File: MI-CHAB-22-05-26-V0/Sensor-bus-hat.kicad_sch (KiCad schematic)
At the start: 45 parts, among them J6 Coaxial_Small, Q2 IRLML6244, U1 MS860702BA01-50, U2 LMT84DCK, U3 BNO085, U4 AP2112K-1.8, U5 LMT84DCK, U6 TPS3850H50DRCR, U7 MAX-M10M-00B, Y1 9HT10-32.768KBZF-T

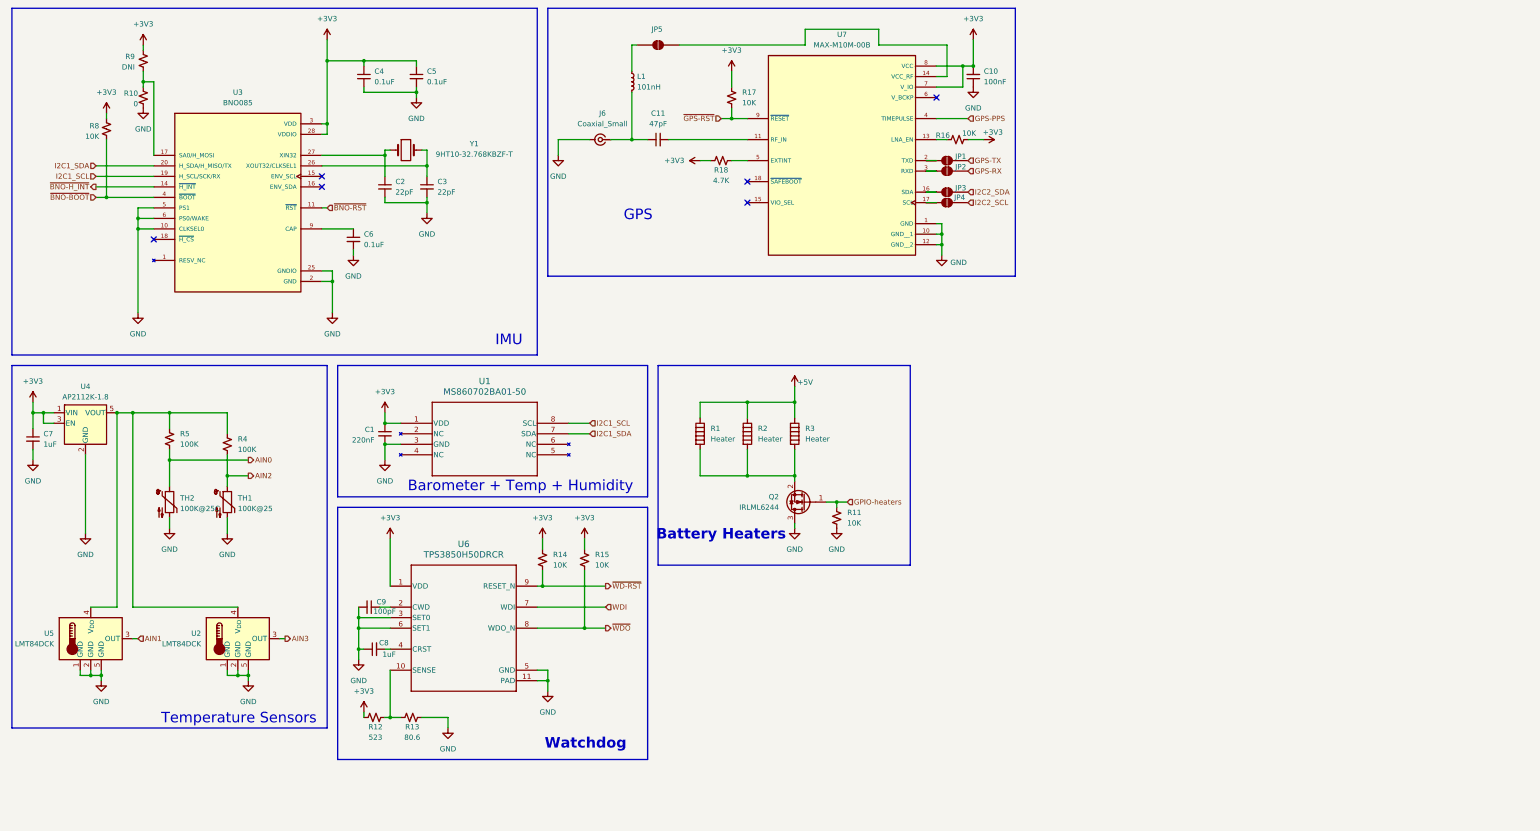
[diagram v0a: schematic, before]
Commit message: revision 0.1 - added debug stuff, CAN interface, I2C buffer
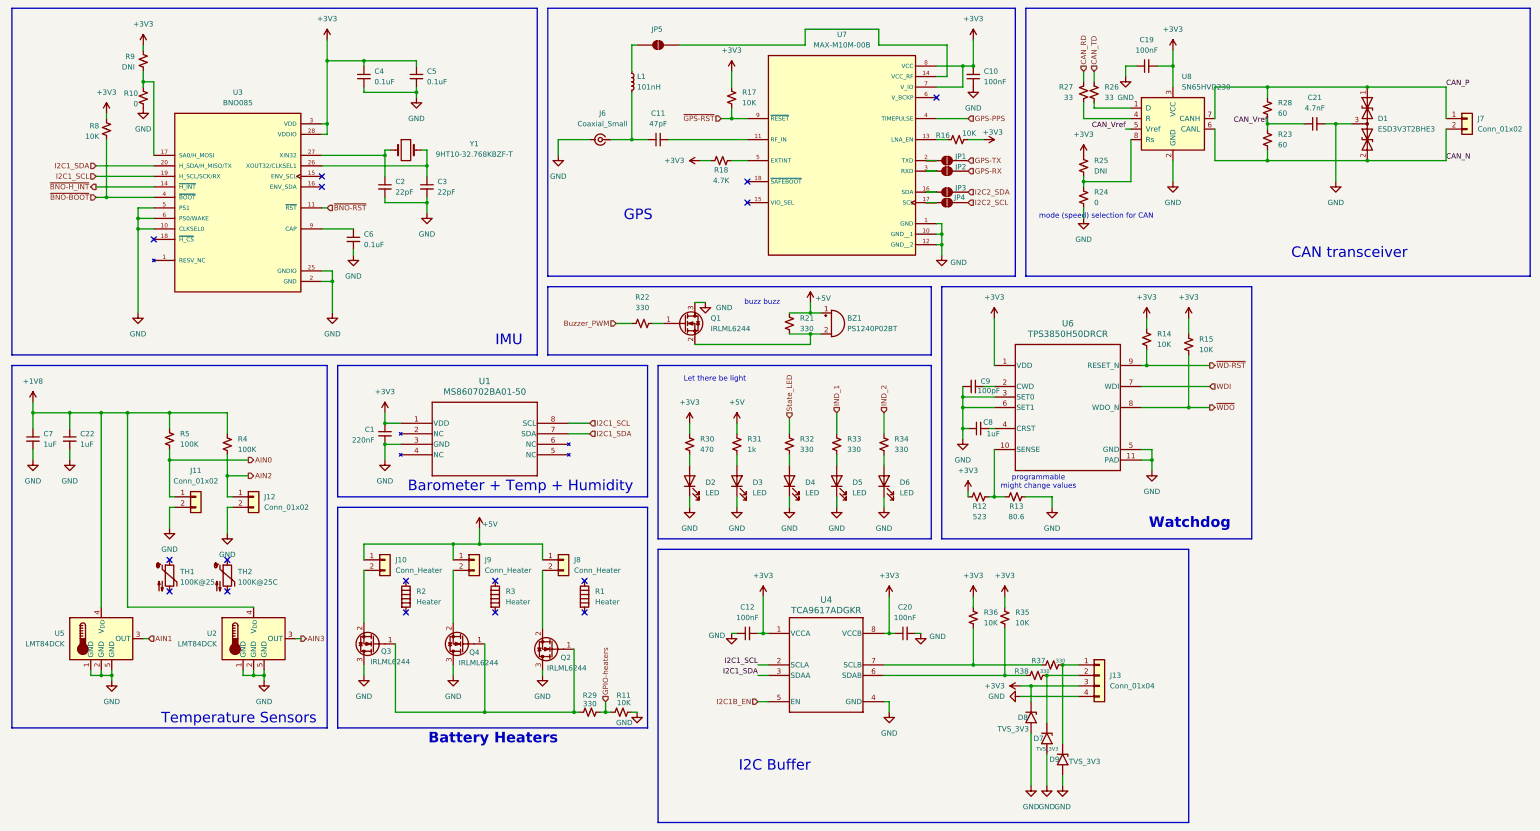
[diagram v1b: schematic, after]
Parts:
- removed U4: AP2112K-1.8, Package_TO_SOT_SMD:SOT-23-5, symbol Regulator_Linear:AP2112K-1.8
- added BZ1: PS1240P02BT, symbol Device:Buzzer
- added C12, C19, C20: 100nF, symbol Device:C_Small
- added C21: 4.7nF, symbol Device:C_Small
- added C22: 1uF, symbol Device:C_Small
- added D1: ESD3V3T2BHE3, Package_TO_SOT_SMD:SOT-23, symbol Diode:SM712_SOT23
- added D2, D3, D4, D5, D6: LED, symbol Device:LED
- added D7, D8, D9: TVS_3V3, Diode_SMD:D_SMB, symbol Diode:SM6T33A
- added J10, J8, J9: Conn_Heater, symbol Connector_Generic:Conn_01x02
- added J11, J12, J7: Conn_01x02, symbol Connector_Generic:Conn_01x02
- added J13: Conn_01x04, symbol Connector_Generic:Conn_01x04
- added Q1, Q3, Q4: IRLML6244, Package_TO_SOT_SMD:SOT-23, symbol Transistor_FET:IRLML6244
- added R21, R22, R29, R32, R33, R34, R37, R38: 330, symbol Device:R_Small_US
- added R23, R28: 60, symbol Device:R_Small_US
- added R24: 0, symbol Device:R_Small_US
- added R25: DNI, symbol Device:R_Small_US
- added R26, R27: 33, symbol Device:R_Small_US
- added R30: 470, symbol Device:R_Small_US
- added R31: 1k, symbol Device:R_Small_US
- added R35, R36: 10K, symbol Device:R_Small_US
- added U4: TCA9617ADGKR, DGK0008A, symbol 2026-03-24_01-09-19:TCA9617ADGKR
- added U8: SN65HVD230, Package_SO:SOIC-8_3.9x4.9mm_P1.27mm, symbol Interface_CAN_LIN:SN65HVD230
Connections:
- net +3V3: now also C12.2, C19.2, C20.1, D8.1 (A1), J13.3 (Pin_3), R25.1, R30.1, R35.1, R36.1, U4.1 (VCCA), U4.8 (VCCB), U8.3 (VCC); no longer C7.1
- net +5V: now also BZ1.1 (+), J10.1 (Pin_1), J8.1 (Pin_1), J9.1 (Pin_1), R21.1, R31.1; no longer R1.1, R2.1, R3.1
- net AIN0: now also J11.1 (Pin_1); no longer TH2.1
- net AIN2: now also J12.1 (Pin_1); no longer TH1.1
- net GND: now also C12.1, C19.1, C20.2, C21.2, C22.2, D1.3 (common), D2.1 (K), D3.1 (K), D4.1 (K), D5.1 (K), D6.1 (K), D7.2 (A2), D8.2 (A2), D9.2 (A2), J11.2 (Pin_2), J12.2 (Pin_2), J13.4 (Pin_4), Q1.3 (D), Q3.3 (D), Q4.3 (D), R24.2, U4.4 (GND), U8.2 (GND); no longer TH1.2, TH2.2
- net GPIO-heaters: now also R29.1; no longer Q2.1 (G)
- net I2C1_SCL: now also U4.2 (SCLA)
- net I2C1_SDA: now also U4.3 (SDAA)
- net +1V8: now reaches R4.1, R5.1, U2.4 (V_{DD}), U5.4 (V_{DD})
- net +1V8: now also C7.1, C22.1
- new net: R24.1, R25.2, U8.8 (Rs)
- new net: Q2.1 (G), Q3.1 (G), Q4.1 (G), R29.2
- new net: R26.2, U8.1 (D)
- new net: BZ1.2 (-), Q1.2 (S), R21.2
- new net: R35.2, R38.1, U4.6 (SDAB)
- new net: J9.2 (Pin_2), Q4.2 (S)
- new net: D2.2 (A), R30.2
- new net: Q1.1 (G), R22.2
- new net: R27.2, U8.4 (R)
- new net: R36.2, R37.1, U4.7 (SCLB)
- new net: J10.2 (Pin_2), Q3.2 (S)
- new net: D5.2 (A), R33.2
- new net: D7.1 (A1), J13.2 (Pin_2), R38.2
- new net: D3.2 (A), R31.2
- new net: J8.2 (Pin_2), Q2.2 (S)
- new net: D6.2 (A), R34.2
- new net: D9.1 (A1), J13.1 (Pin_1), R37.2
- new net: D4.2 (A), R32.2
- new net Buzzer_PWM: R22.1
- new net CAN_N: D1.2 (A2), J7.2 (Pin_2), R23.2, U8.6 (CANL)
- new net CAN_P: D1.1 (A1), J7.1 (Pin_1), R28.1, U8.7 (CANH)
- new net CAN_RD: R27.1
- new net CAN_TD: R26.1
- new net CAN_Vref: C21.1, R23.1, R28.2, U8.5 (Vref)
- new net I2C1B_EN: U4.5 (EN)
- new net IND_1: R33.1
- new net IND_2: R34.1
- new net State_LED: R32.1
- now unconnected: R1.2, R2.2, R3.2
- no-connect marks 6 -> 16
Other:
- note added: "CAN transceiver"
- note added: "I2C Buffer"
- note added: "Let there be light"
- note added: "buzz buzz"
- note added: "mode (speed) selection for CAN"
- note added: "programmable might change values"
- moved on the sheet: C8, C9, Q2, R11, R12, R13, R14, R15, TH1, TH2, U2, U5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
